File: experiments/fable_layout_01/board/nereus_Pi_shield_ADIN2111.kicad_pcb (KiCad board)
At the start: 6 copper layers, 46 x 65 mm, 138 parts, among them J1 Raspberry_Pi_2_3, J5 SM02B-GHS-TB, T1 74930000, T2 74930000, U1 ADIN2111BCPZ, U10 LMR51430YDDCR, U11 TPS26621DRCR, U2 AP22913CN4-7, U3 AP22913CN4-7, U4 INA232AIDDFR, U5 LMR51430YDDCR, U6 TPS62840YBGR, Y1 ABM11W-25.0000MHZ-6-K1Z-T3

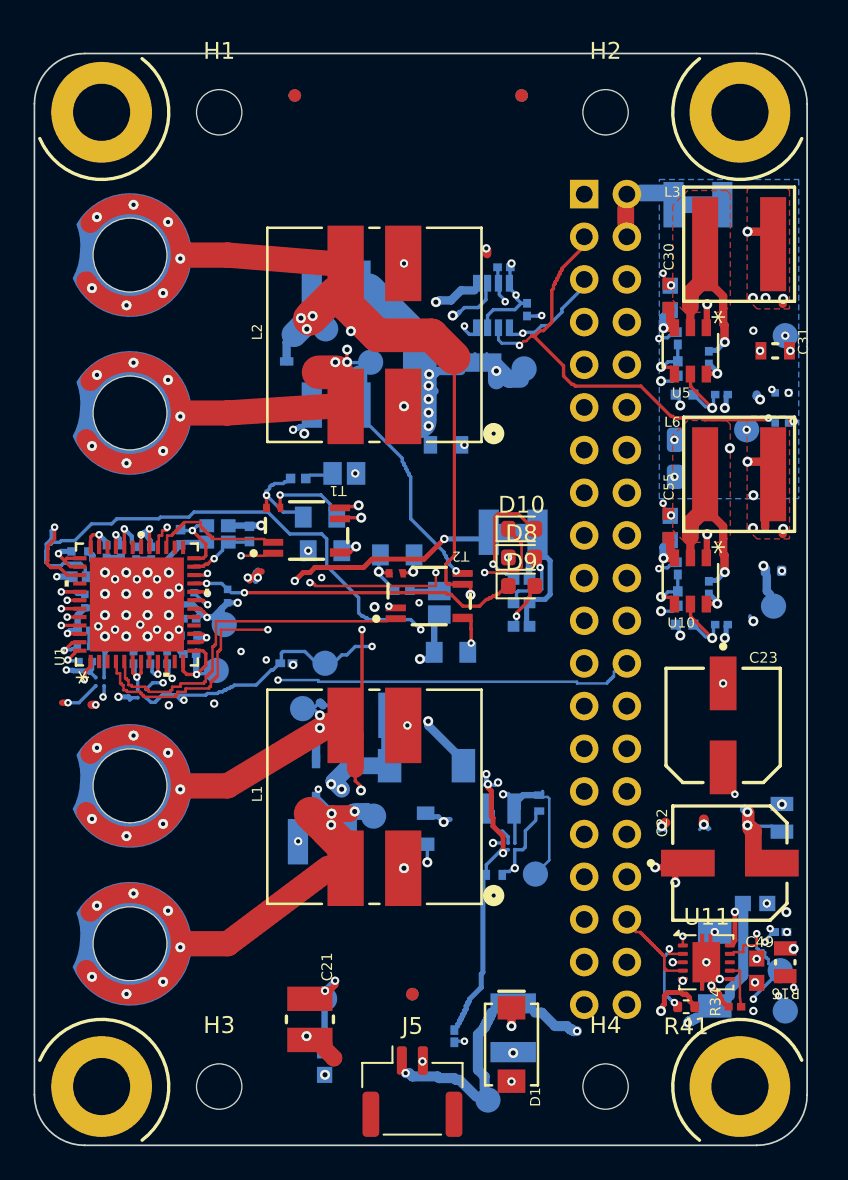
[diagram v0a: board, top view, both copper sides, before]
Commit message: fable layout 01 S7.b round 2: Kelvin sense traces restored, bus rule as a .kicad_dru enforced by DRC, cross-class clearance in the router
- SENSE region gains the Kelvin detour (Bottom); traces protected; pad-to-pad check in check_rules
- bus nets 0.35 from non-bus nets (board rule); router kind map; power fallbacks keep 0.25
- 1V8 at 0.15 from one bus-leg via, declared and excluded; plane nets pre-stitched
- DRC 111 (110 Sofar + 1 declared), 0 copper-defect warnings, 1 open (J1 by design)
- QE round-2 report saved to experiments/fable_layout_01/qe/S7b_round2.md

Co-Authored-By: Claude Fable 5.1 <noreply@anthropic.com>
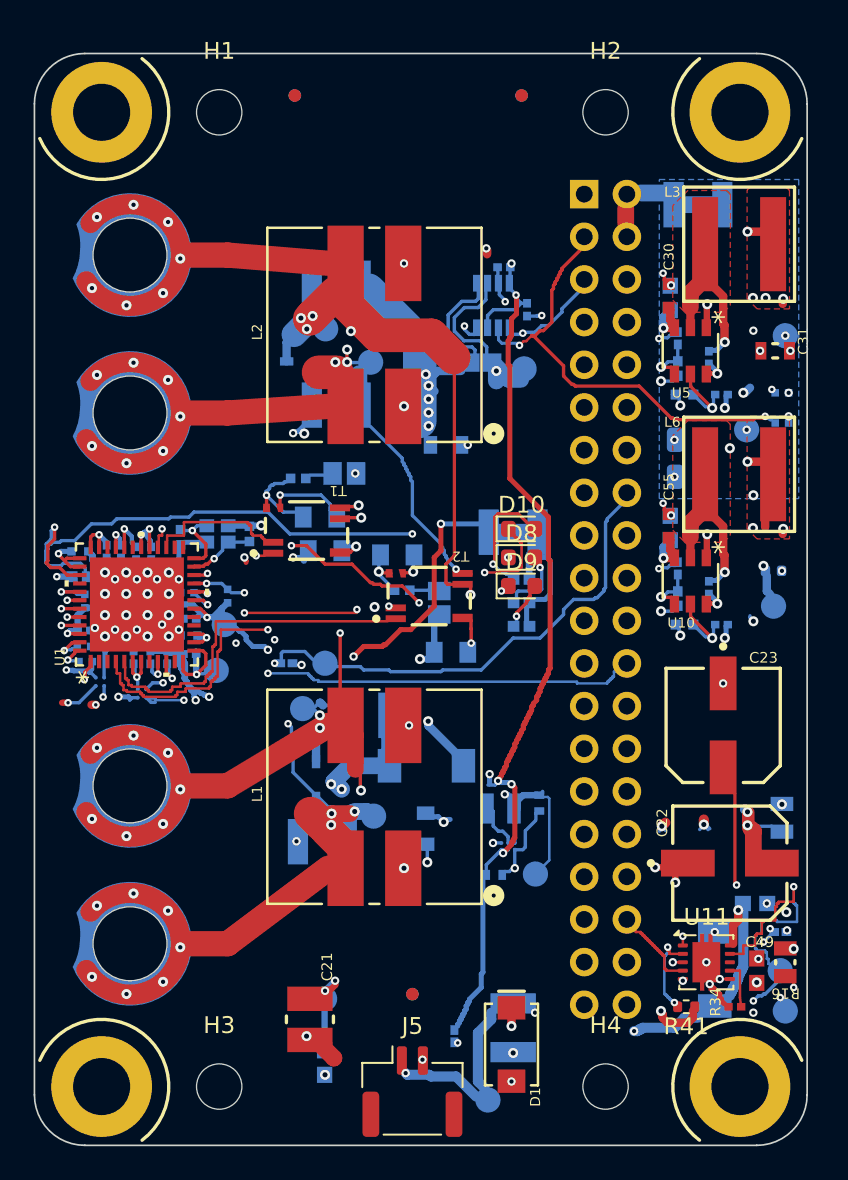
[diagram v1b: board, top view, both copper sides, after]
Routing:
- net /Top-Level Schematic/~{PAYLOAD_FAULT}: track 25.4 -> 36.6 mm
- net ADIN_VDDIO: track 34.5 -> 39.4 mm
- net VBUS: track 34.2 -> 38.3 mm, vias 22 -> 21
- net /Top-Level Schematic/PoDL/Power Monitor/P_IN: track 15.1 -> 19.0 mm, vias 7 -> 6
- net GND: track 70.2 -> 74.0 mm, vias 85 -> 86
- net 3V3: track 108.2 -> 110.7 mm, vias 17 -> 16
- net /Top-Level Schematic/ADIN_PWR: track 44.0 -> 46.0 mm
- net /Top-Level Schematic/ADIN_MOSI: track 36.5 -> 35.1 mm
- net /Top-Level Schematic/BM1_N: track 51.0 -> 52.4 mm
- net /Top-Level Schematic/~{ADIN_INT}: track 50.7 -> 49.3 mm
- net /Top-Level Schematic/ADIN/~{ADIN_P1_LED1}: track 18.9 -> 19.1 mm, vias 2 -> 3
- net 1V8: vias 3 -> 2

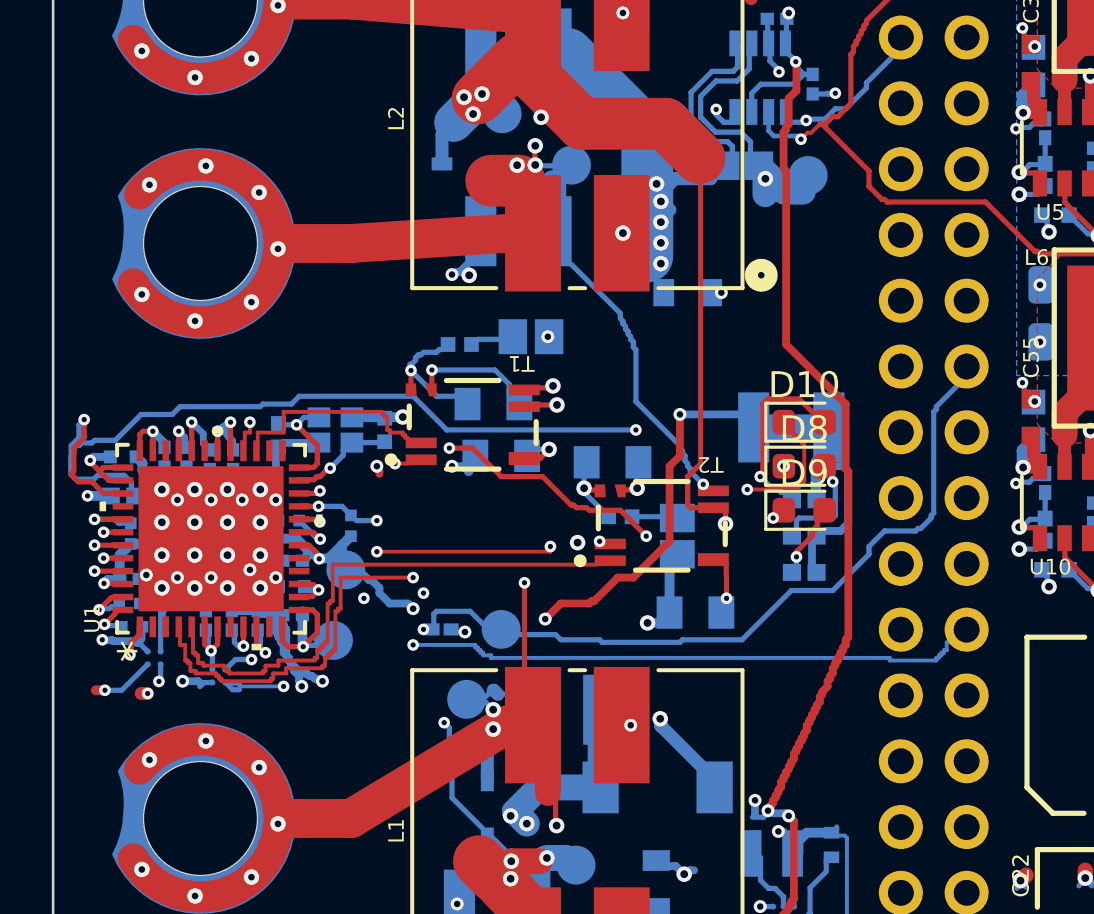
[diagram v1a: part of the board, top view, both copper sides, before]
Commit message: fable layout 01 S7.b round 3: REPORT §5/§6 restored; new bus legs keep 0.35 from the opposite leg (busleg class, soft pad goals)
- QE round-3 report saved to experiments/fable_layout_01/qe/S7b_round3.md
- DRC 111 (110 Sofar + 1 declared), 0 copper-defect warnings, 1 open (J1 by design), Kelvin both links

Co-Authored-By: Claude Fable 5.1 <noreply@anthropic.com>
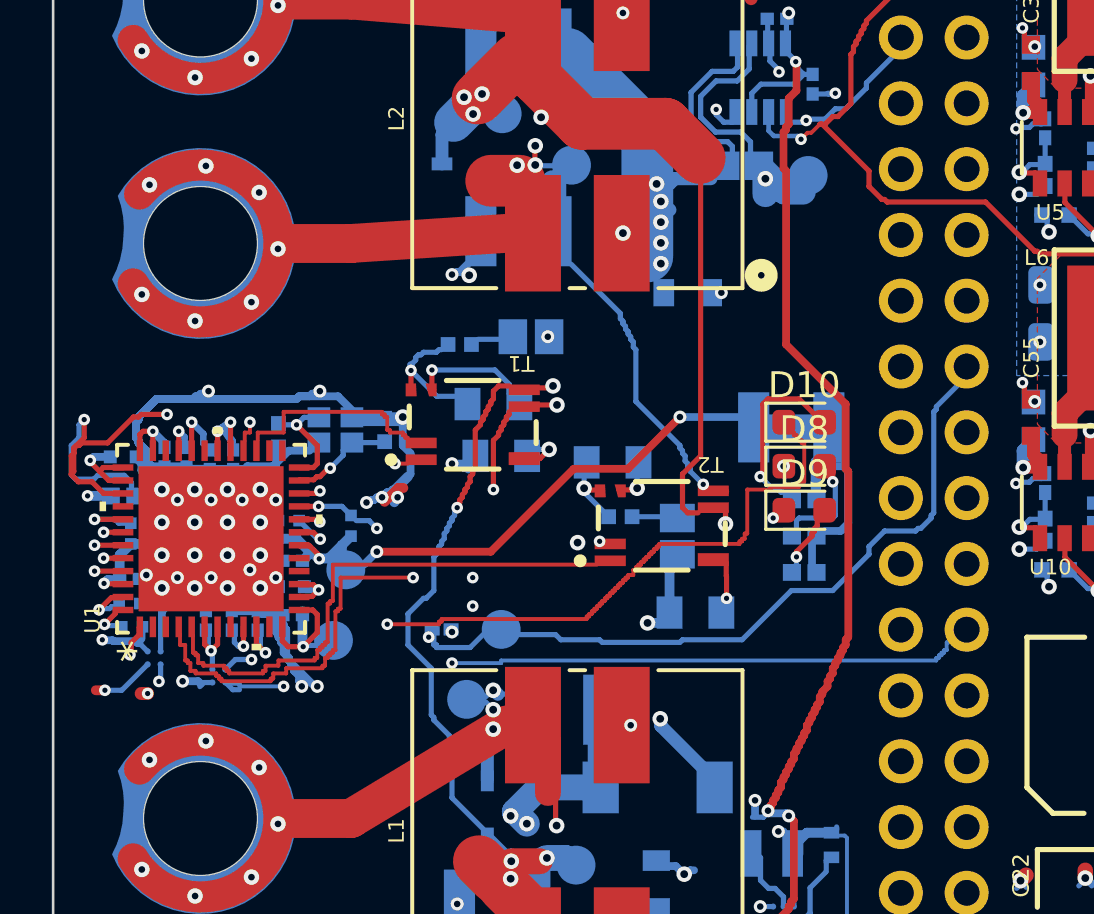
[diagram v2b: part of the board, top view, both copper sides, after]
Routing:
- net GND: track 74.0 -> 120.5 mm, vias 86 -> 90
- net ADIN_VDDIO: track 39.4 -> 35.0 mm, vias 7 -> 6
- net 3V3: track 110.7 -> 112.0 mm
- net /Top-Level Schematic/~{ADIN_INT}: track 49.3 -> 48.5 mm
- net /Top-Level Schematic/ADIN_MOSI: track 35.1 -> 35.9 mm, vias 3 -> 2
- net /Top-Level Schematic/ADIN_SCK: track 32.8 -> 32.1 mm
- net /Top-Level Schematic/BM1_N: track 52.4 -> 52.9 mm
- net /Top-Level Schematic/BM1_P: track 41.6 -> 41.7 mm, vias 12 -> 13
- net /Top-Level Schematic/ADIN/~{ADIN_P2_LED1}: vias 3 -> 2
- net /Top-Level Schematic/ADIN_MISO: vias 3 -> 1
